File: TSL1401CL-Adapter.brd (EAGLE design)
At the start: 30.5 x 30.5 mm, 4 parts

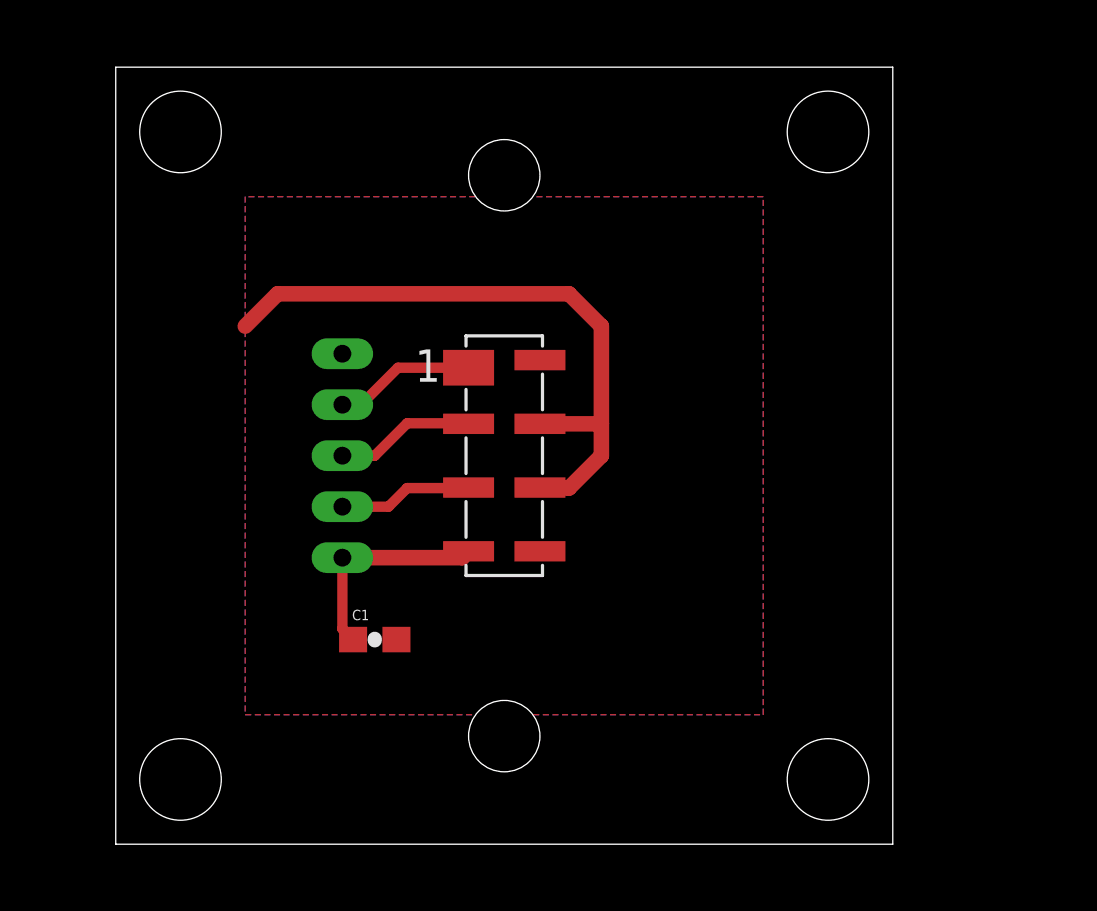
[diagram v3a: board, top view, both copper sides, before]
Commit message: Switched to 1/8" Via instead of a normal drill hole to help with grounding to a case
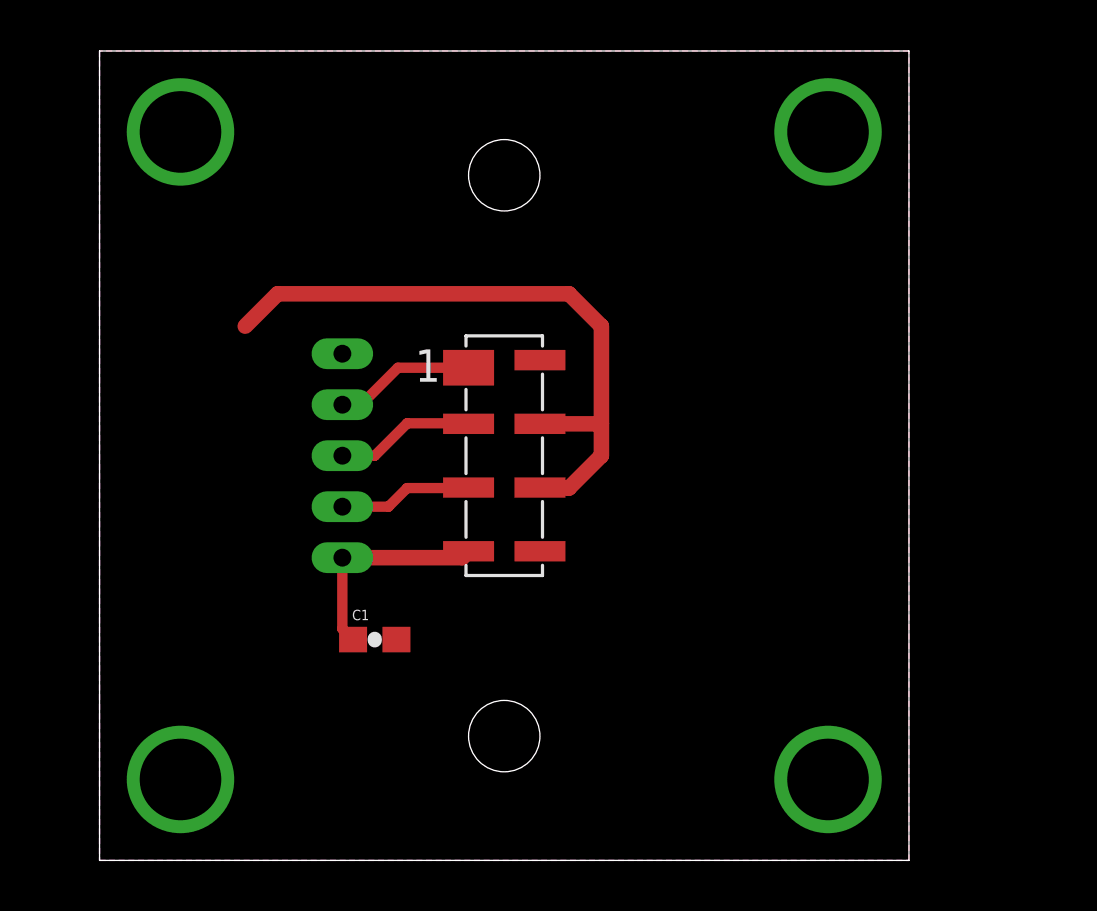
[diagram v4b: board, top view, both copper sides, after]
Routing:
- net GND: vias 0 -> 4
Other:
- board size 30.5 x 30.5 mm -> 31.8 x 31.8 mm
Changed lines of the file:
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@@
 <?xml version="1.0" encoding="utf-8"?>
 <!DOCTYPE eagle SYSTEM "eagle.dtd">
-<eagle version="6.3">
+<eagle version="6.4">
 <drawing>
 <settings>
@@
 <layer number="22" name="bPlace" color="14" fill="1" visible="yes" active="yes"/>
 <layer number="23" name="tOrigins" color="15" fill="1" visible="yes" active="yes"/>
-<layer number="24" name="bOrigins" color="15" fill="1" visible="yes" active="yes"/>
+<layer number="24" name="bOrigins" color="15" fill="1" visible="no" active="yes"/>
 <layer number="25" name="tNames" color="7" fill="1" visible="yes" active="yes"/>
-<layer number="26" name="bNames" color="7" fill="1" visible="yes" active="yes"/>
+<layer number="26" name="bNames" color="7" fill="1" visible="no" active="yes"/>
 <layer number="27" name="tValues" color="7" fill="1" visible="no" active="yes"/>
 <layer number="28" name="bValues" color="7" fill="1" visible="no" active="yes"/>
@@
 <layer number="39" name="tKeepout" color="4" fill="11" visible="no" active="yes"/>
 <layer number="40" name="bKeepout" color="1" fill="11" visible="no" active="yes"/>
-<layer number="41" name="tRestrict" color="4" fill="10" visible="yes" active="yes"/>
+<layer number="41" name="tRestrict" color="4" fill="10" visible="no" active="yes"/>
 <layer number="42" name="bRestrict" color="1" fill="10" visible="no" active="yes"/>
 <layer number="43" name="vRestrict" color="2" fill="10" visible="no" active="yes"/>
@@
 <layer number="50" name="dxf" color="7" fill="1" visible="no" active="yes"/>
 <layer number="51" name="tDocu" color="6" fill="1" visible="yes" active="yes"/>
-<layer number="52" name="bDocu" color="7" fill="1" visible="yes" active="yes"/>
+<layer number="52" name="bDocu" color="7" fill="1" visible="no" active="yes"/>
 <layer number="53" name="tGND_GNDA" color="7" fill="9" visible="no" active="no"/>
 <layer number="54" name="bGND_GNDA" color="1" fill="9" visible="no" active="no"/>
@@
 <board>
 <plain>
-<wire x1="0" y1="0" x2="30.48" y2="0" width="0" layer="20"/>
-<wire x1="30.48" y1="0" x2="30.48" y2="30.48" width="0" layer="20"/>
-<wire x1="30.48" y1="30.48" x2="0" y2="30.48" width="0" layer="20"/>
-<wire x1="0" y1="30.48" x2="0" y2="0" width="0" layer="20"/>
+<wire x1="-0.635" y1="-0.635" x2="31.115" y2="-0.635" width="0" layer="20"/>
+<wire x1="31.115" y1="-0.635" x2="31.115" y2="31.115" width="0" layer="20"/>
+<wire x1="31.115" y1="31.115" x2="-0.635" y2="31.115" width="0" layer="20"/>
+<wire x1="-0.635" y1="31.115" x2="-0.635" y2="-0.635" width="0" layer="20"/>
 <text x="24.765" y="28.956" size="1.27" layer="22" font="vector" ratio="15" rot="MR0">TSL1401CL Adapter</text>
 <text x="24.13" y="3.81" size="1.016" layer="22" font="vector" ratio="15" rot="MR90">Karl Bellve</text>
@@
 <text x="19.05" y="3.81" size="1.016" layer="22" font="vector" ratio="15" rot="MR90">Medical School</text>
 <text x="17.78" y="3.81" size="1.016" layer="22" font="vector" ratio="15" rot="MR90">March 28, 2013</text>
-<hole x="2.54" y="27.94" drill="3.2"/>
-<hole x="2.54" y="2.54" drill="3.2"/>
-<hole x="27.94" y="27.94" drill="3.2"/>
-<hole x="27.94" y="2.54" drill="3.2"/>
-<dimension x1="27.94" y1="27.94" x2="27.94" y2="2.54" x3="35.56" y3="15.24" layer="51" dtype="vertical"/>
-<dimension x1="15.24" y1="15.24" x2="0" y2="15.24" x3="7.62" y3="33.02" layer="51" dtype="vertical"/>
-<dimension x1="15.24" y1="15.24" x2="15.24" y2="30.48" x3="-2.54" y3="22.86" layer="51" dtype="vertical"/>
+<dimension x1="27.94" y1="27.94" x2="27.94" y2="2.54" x3="34.29" y3="15.24" textsize="1.778" layer="51" dtype="vertical"/>
+<dimension x1="15.24" y1="15.24" x2="-0.635" y2="15.24" x3="7.3025" y3="33.02" textsize="1.778" layer="51" dtype="vertical"/>
+<dimension x1="15.24" y1="15.24" x2="15.367" y2="31.115" x3="-6.35" y3="23.1775" textsize="1.778" layer="51" dtype="vertical"/>
 <text x="16.002" y="18.542" size="1.27" layer="22" rot="MR0">GND</text>
 <text x="16.129" y="12.7" size="1.27" layer="22" rot="MR0">AO</text>
@@
 <text x="16.002" y="14.605" size="1.27" layer="22" rot="MR0">CLK</text>
 <text x="16.129" y="10.541" size="1.27" layer="22" rot="MR0">5V</text>
-<dimension x1="15.24" y1="15.24" x2="2.54" y2="27.94" x3="-8.89" y3="21.59" layer="51" dtype="vertical"/>
-<dimension x1="15.24" y1="15.24" x2="27.94" y2="15.24" x3="21.59" y3="-2.54" layer="51" dtype="horizontal"/>
-<dimension x1="0" y1="0" x2="30.48" y2="0" x3="15.24" y3="-8.89" layer="51" dtype="horizontal"/>
+<dimension x1="15.24" y1="15.24" x2="2.54" y2="27.94" x3="-2.54" y3="21.59" textsize="1.778" layer="51" dtype="vertical"/>
+<dimension x1="15.24" y1="15.24" x2="27.94" y2="15.24" x3="21.59" y3="-3.81" textsize="1.778" layer="51" dtype="horizontal"/>
+<dimension x1="-0.635" y1="0.127" x2="31.115" y2="0" x3="15.24" y3="-8.89" textsize="1.778" layer="51" dtype="horizontal"/>
 </plain>
 <attributes>
@@
 <signal name="GND">
 <polygon width="0.4064" layer="1">
-<vertex x="5.08" y="25.4"/>
-<vertex x="5.08" y="5.08"/>
-<vertex x="25.4" y="5.08"/>
-<vertex x="25.4" y="25.4"/>
+<vertex x="-0.635" y="31.115"/>
+<vertex x="-0.635" y="-0.635"/>
+<vertex x="31.115" y="-0.635"/>
+<vertex x="31.115" y="31.115"/>
 </polygon>
 <polygon width="0.4064" layer="16">
-<vertex x="5.08" y="25.4"/>
-<vertex x="5.08" y="5.08"/>
-<vertex x="25.4" y="5.08"/>
-<vertex x="25.4" y="25.4"/>
+<vertex x="-0.635" y="31.115"/>
+<vertex x="-0.635" y="-0.635"/>
+<vertex x="31.115" y="-0.635"/>
+<vertex x="31.115" y="31.115"/>
 </polygon>
 <contactref element="C1" pad="2"/>
@@
 <wire x1="19.03" y1="16.49" x2="19.05" y2="16.51" width="0.6096" layer="1"/>
 <contactref element="U$3" pad="P$1"/>
+<via x="2.54" y="27.94" extent="1-16" drill="3.2"/>
+<via x="2.54" y="2.54" extent="1-16" drill="3.2"/>
+<via x="27.94" y="27.94" extent="1-16" drill="3.2"/>
+<via x="27.94" y="2.54" extent="1-16" drill="3.2"/>
 </signal>
 <signal name="SI">
